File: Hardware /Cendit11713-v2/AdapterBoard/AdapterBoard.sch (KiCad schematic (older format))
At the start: 5 parts, among them J1 BOARD_EDGE_22P, J2 PIN_HEADER_01X22, J3 SLIMLINE_SATA_PLUG_7P_6P_HORZ, J4 SATA_RECEPTACLE_VERTICAL_SMT_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, J5 SATA_BACKPLANE_RECEPTACLE_VER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

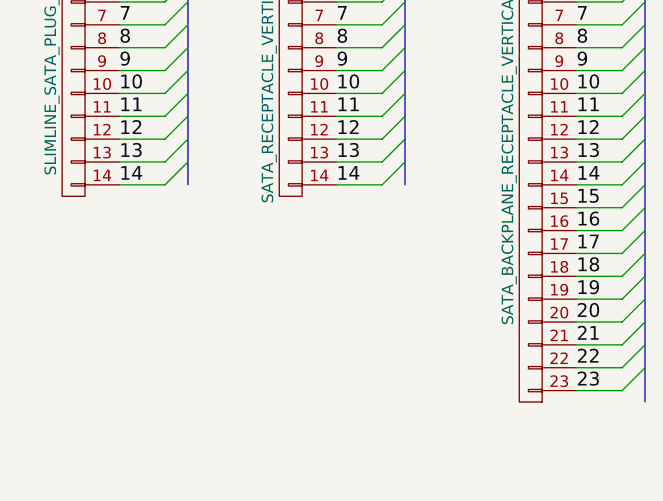
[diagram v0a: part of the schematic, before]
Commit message: Trabajo en CenditLab.Reducido + Cendit17713 PCB
  - Clases paneles UI modificados
  - Clases para manejo y validacion de datos
  - PCB expansor puertos Viking
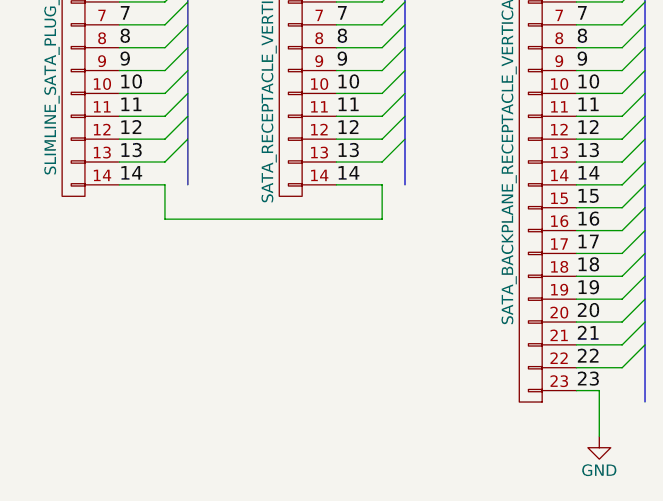
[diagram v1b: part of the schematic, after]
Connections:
- net 23 renamed GND
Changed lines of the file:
@@
 LIBS:74xx
 LIBS:cmos4000
-LIBS:CenditBasic
+LIBS:AdapterBoard-cache
 EELAYER 25 0
 EELAYER END
@@
 	3000 2300 3200 2300
 Entry Wire Line
-	3200 2300 3300 2200
-Entry Wire Line
 	3200 2200 3300 2100
 Wire Wire Line
@@
 	3950 2300 4150 2300
 Entry Wire Line
-	4150 2300 4250 2200
-Entry Wire Line
 	4150 2200 4250 2100
 Wire Wire Line
@@
 Entry Wire Line
 	5200 2800 5300 2700
-Wire Wire Line
-	5000 3200 5200 3200
-Entry Wire Line
-	5200 3200 5300 3100
 Wire Bus Line
 	2300 3050 2300 650
@@
 Wire Bus Line
 	1250 2950 1250 650
+Wire Wire Line
+	4150 2300 4150 2450
+Wire Wire Line
+	4150 2450 3200 2450
+Wire Wire Line
+	3200 2450 3200 2300
+$Comp
+L GND #PWR01
+U 1 1 59DEB810
+P 5100 3400
+F 0 "#PWR01" H 5100 3150 50  0001 C CNN
+F 1 "GND" H 5100 3250 50  0000 C CNN
+F 2 "" H 5100 3400 50  0000 C CNN
+F 3 "" H 5100 3400 50  0000 C CNN
+	1    5100 3400
+	1    0    0    -1
+$EndComp
+Wire Wire Line
+	5000 3200 5100 3200
+Wire Wire Line
+	5100 3200 5100 3400
 $EndSCHEMATC
